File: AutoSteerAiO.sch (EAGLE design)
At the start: 81 parts, among them IC2 MMA8452Q, J4 CONNECTOR 1x5 PINS, K4 CB1A-P-12V

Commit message: Add files via upload
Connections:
- net HIGH: now also ADS1115.A0, C14.2, R11.2; no longer ADS1115.A1, C13.2, R10.2
- net HIGH.: now also R11.1, R4.1, WAS_D.3; no longer R10.1, WAS_D.4
- net LOW: now also ADS1115.A1, C13.2, R10.2; no longer ADS1115.A0, C14.2, R11.2
- net LOW.: now also R10.1, WAS_D.4; no longer R11.1, R4.1, WAS_D.3
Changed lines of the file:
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@@
 </segment>
 </net>
-<net name="LOW." class="0">
+<net name="HIGH." class="0">
 <segment>
 <pinref part="WAS_D" gate="G$1" pin="3"/>
@@
 </segment>
 </net>
-<net name="HIGH." class="0">
+<net name="LOW." class="0">
 <segment>
 <pinref part="WAS_D" gate="G$1" pin="4"/>
@@
 <net name="HIGH" class="0">
 <segment>
-<pinref part="ADS1115" gate="G$1" pin="A1"/>
-<wire x1="190.5" y1="284.48" x2="195.58" y2="284.48" width="0.1524" layer="91"/>
-<label x="198.12" y="284.48" size="1.778" layer="95" rot="R180" align="top-left"/>
-</segment>
-<segment>
-<pinref part="R10" gate="G$1" pin="2"/>
-<wire x1="213.36" y1="254" x2="236.22" y2="254" width="0.1524" layer="91"/>
-<pinref part="C13" gate="G$1" pin="2"/>
-<wire x1="236.22" y1="254" x2="236.22" y2="248.92" width="0.1524" layer="91"/>
-</segment>
-</net>
-<net name="LOW" class="0">
-<segment>
 <pinref part="ADS1115" gate="G$1" pin="A0"/>
 <wire x1="190.5" y1="281.94" x2="195.58" y2="281.94" width="0.1524" layer="91"/>
@@
 <wire x1="213.36" y1="250.19" x2="228.6" y2="250.19" width="0.1524" layer="91"/>
 <wire x1="228.6" y1="250.19" x2="228.6" y2="248.92" width="0.1524" layer="91"/>
-</segment>
-</net>
+<label x="226.06" y="256.54" size="1.778" layer="95"/>
+</segment>
+</net>
+<net name="LOW" class="0">
+<segment>
+<pinref part="ADS1115" gate="G$1" pin="A1"/>
+<wire x1="190.5" y1="284.48" x2="195.58" y2="284.48" width="0.1524" layer="91"/>
+<label x="198.12" y="284.48" size="1.778" layer="95" rot="R180" align="top-left"/>
+</segment>
+<segment>
+<pinref part="R10" gate="G$1" pin="2"/>
+<wire x1="213.36" y1="254" x2="236.22" y2="254" width="0.1524" layer="91"/>
+<pinref part="C13" gate="G$1" pin="2"/>
+<wire x1="236.22" y1="254" x2="236.22" y2="248.92" width="0.1524" layer="91"/>
+<label x="215.9" y="256.54" size="1.778" layer="95"/>
+</segment>
+</net>

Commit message: Add files via upload
silkscreen edit
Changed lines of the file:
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@@
 <wire x1="218.44" y1="223.52" x2="213.36" y2="223.52" width="0.1524" layer="91"/>
 <wire x1="213.36" y1="223.52" x2="213.36" y2="220.98" width="0.1524" layer="91"/>
-<wire x1="213.36" y1="223.52" x2="203.2" y2="223.52" width="0.1524" layer="91"/>
+<wire x1="213.36" y1="223.52" x2="205.74" y2="223.52" width="0.1524" layer="91"/>
 <junction x="213.36" y="223.52"/>
-<label x="203.2" y="223.52" size="1.778" layer="95"/>
+<label x="205.74" y="223.52" size="1.778" layer="95"/>
 </segment>
 </net>

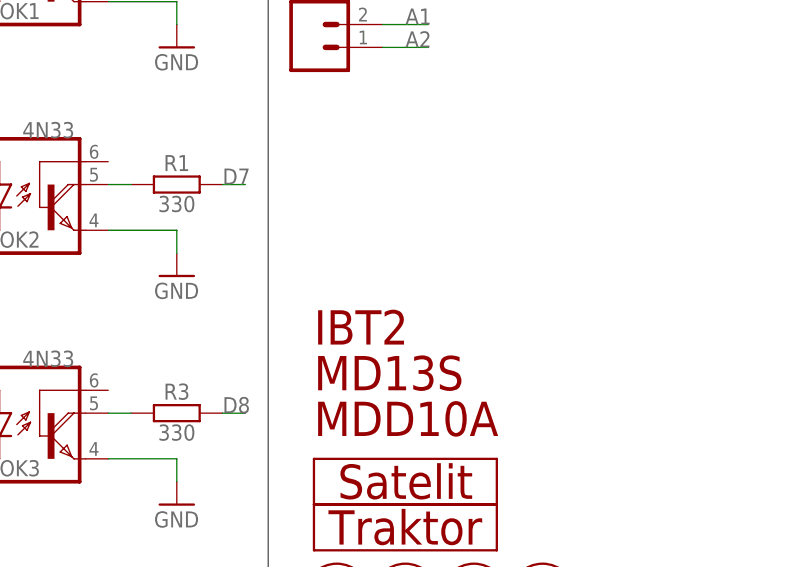
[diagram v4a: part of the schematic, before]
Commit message: Add files via upload
Added MD10C driver
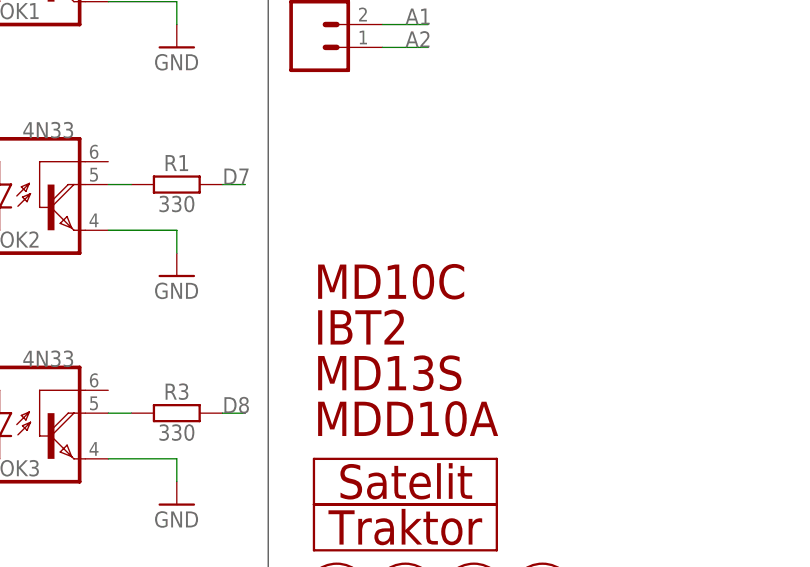
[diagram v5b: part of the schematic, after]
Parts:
- added U$3: MD10C, #Motor Drivers:MD10C
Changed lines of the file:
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@@
 <attribute name="OC_NEWARK" value="unknown"/>
 </part>
-<part name="U$8" library="#Logo" library_urn="urn:adsk.eagle:library:8978129" deviceset="SATELIT-MALI" device="" package3d_urn="urn:adsk.eagle:package:8978137/1">
-<attribute name="MF" value=""/>
-<attribute name="MPN" value=""/>
-<attribute name="OC_NEWARK" value="unknown"/>
-</part>
-<part name="U$5" library="#Logo" library_urn="urn:adsk.eagle:library:8978129" deviceset="TRAKTOR-MALI" device="" package3d_urn="urn:adsk.eagle:package:8978136/1">
-<attribute name="MF" value=""/>
-<attribute name="MPN" value=""/>
-<attribute name="OC_NEWARK" value="unknown"/>
-</part>
-<part name="U$6" library="#Holes" library_urn="urn:adsk.eagle:library:7295050" deviceset="4.2MM-6MM" device="" package3d_urn="urn:adsk.eagle:package:7295057/3">
-<attribute name="MF" value=""/>
-<attribute name="MPN" value=""/>
-<attribute name="OC_NEWARK" value="unknown"/>
-</part>
-<part name="U$7" library="#Holes" library_urn="urn:adsk.eagle:library:7295050" deviceset="4.2MM-6MM" device="" package3d_urn="urn:adsk.eagle:package:7295057/3">
-<attribute name="MF" value=""/>
-<attribute name="MPN" value=""/>
-<attribute name="OC_NEWARK" value="unknown"/>
-</part>
-<part name="U$9" library="#Holes" library_urn="urn:adsk.eagle:library:7295050" deviceset="4.2MM-6MM" device="" package3d_urn="urn:adsk.eagle:package:7295057/3">
-<attribute name="MF" value=""/>
-<attribute name="MPN" value=""/>
-<attribute name="OC_NEWARK" value="unknown"/>
-</part>
-<part name="U$10" library="#Holes" library_urn="urn:adsk.eagle:library:7295050" deviceset="4.2MM-6MM" device="" package3d_urn="urn:adsk.eagle:package:7295057/3">
+<part name="U$8" library="#Logo" deviceset="SATELIT-MALI" device="">
+<attribute name="MF" value=""/>
+<attribute name="MPN" value=""/>
+<attribute name="OC_NEWARK" value="unknown"/>
+</part>
+<part name="U$5" library="#Logo" deviceset="TRAKTOR-MALI" device="">
+<attribute name="MF" value=""/>
+<attribute name="MPN" value=""/>
+<attribute name="OC_NEWARK" value="unknown"/>
+</part>
+<part name="U$6" library="#Holes" deviceset="4.2MM-6MM" device="">
+<attribute name="MF" value=""/>
+<attribute name="MPN" value=""/>
+<attribute name="OC_NEWARK" value="unknown"/>
+</part>
+<part name="U$7" library="#Holes" deviceset="4.2MM-6MM" device="">
+<attribute name="MF" value=""/>
+<attribute name="MPN" value=""/>
+<attribute name="OC_NEWARK" value="unknown"/>
+</part>
+<part name="U$9" library="#Holes" deviceset="4.2MM-6MM" device="">
+<attribute name="MF" value=""/>
+<attribute name="MPN" value=""/>
+<attribute name="OC_NEWARK" value="unknown"/>
+</part>
+<part name="U$10" library="#Holes" deviceset="4.2MM-6MM" device="">
 <attribute name="MF" value=""/>
 <attribute name="MPN" value=""/>
@@
 <attribute name="OC_NEWARK" value="unknown"/>
 </part>
+<part name="U$3" library="#Motor Drivers" deviceset="MD10C" device=""/>
 </parts>
 <sheets>
@@
 <attribute name="MPN" x="147.32" y="231.14" size="1.778" layer="96" display="off"/>
 </instance>
+<instance part="U$3" gate="G$1" x="144.78" y="139.7" smashed="yes"/>
 </instances>
 <busses>
